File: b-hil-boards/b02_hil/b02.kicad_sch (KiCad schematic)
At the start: 43 parts, among them J1 Conn_01x12_Socket, J2 Conn_01x06_Socket, K1 Relay_DPDT, K2 Relay_DPDT, K3 Relay_DPDT, K4 Relay_DPDT, SW1 SW_Push, U1 MAX485E, U2 ULN2003, U3 ADuM1412, U4 ESP32_C3_SuperMini, U5 OLED-128x64-I2C, U6 74LVC2G34, U7 AMS1117-3.3

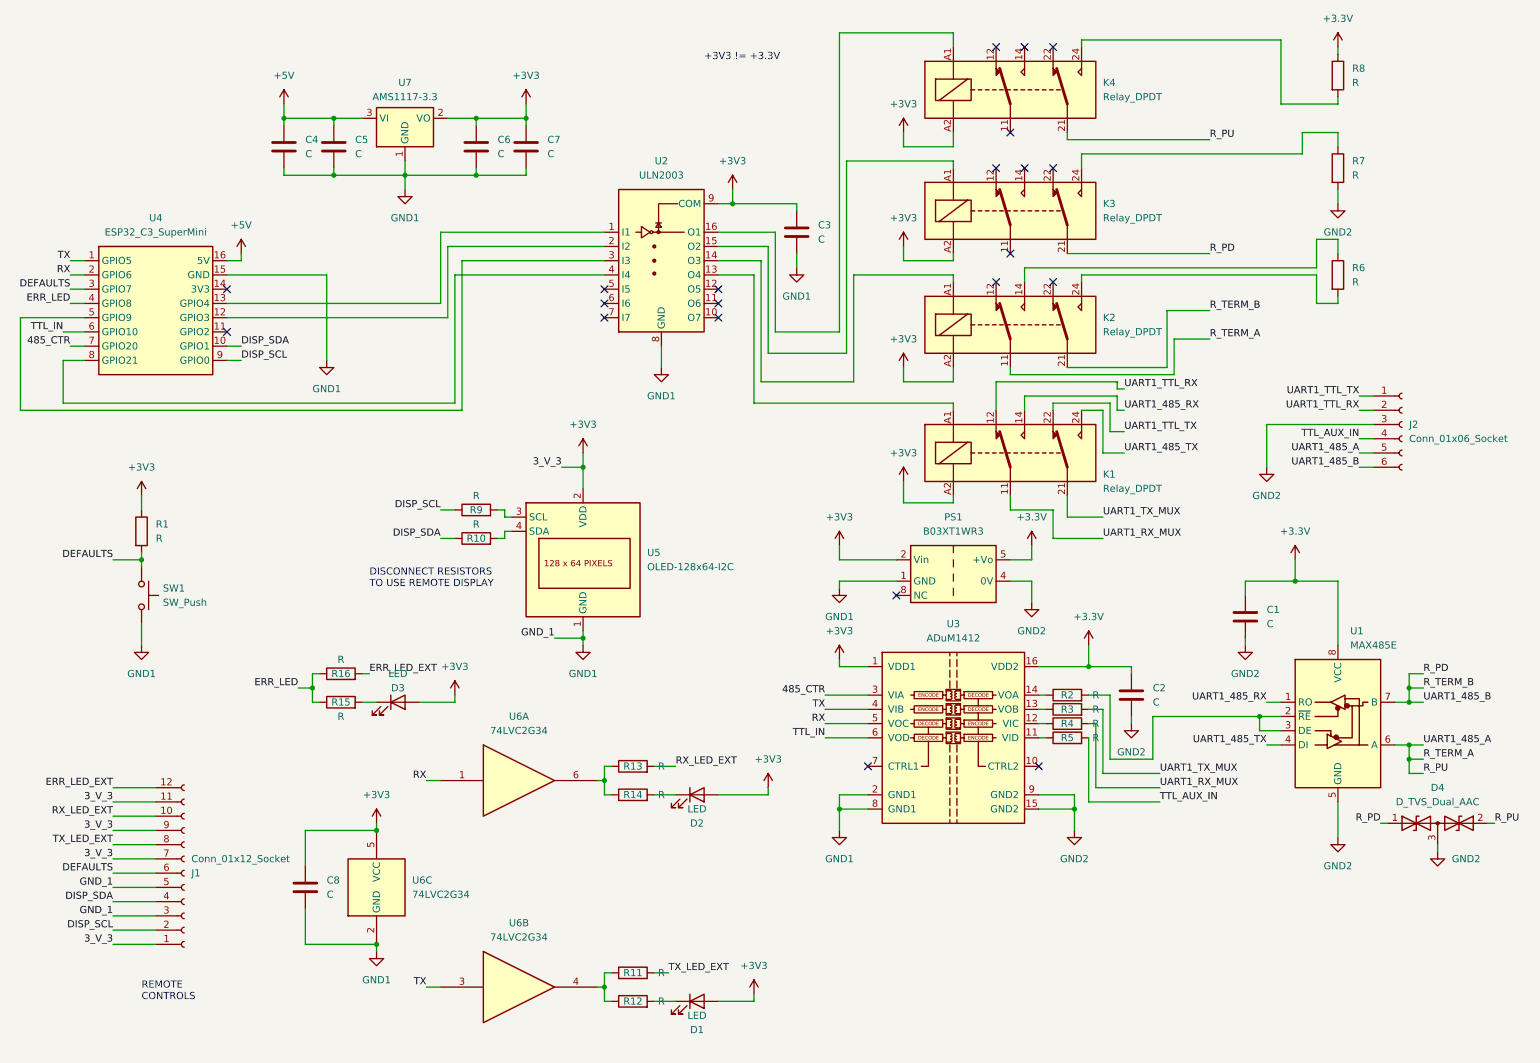
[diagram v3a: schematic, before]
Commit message: B02: add tri-state buffer and re-route PCB
Add 74HCT541 tri-state buffer to the schematic and re-route b02.kicad_pcb
to integrate the new device. Update project layout, refresh FreeRouting
exchange files (b02.dsn, b02.rules, b02.ses), and rotate KiCad automatic
backup archives.
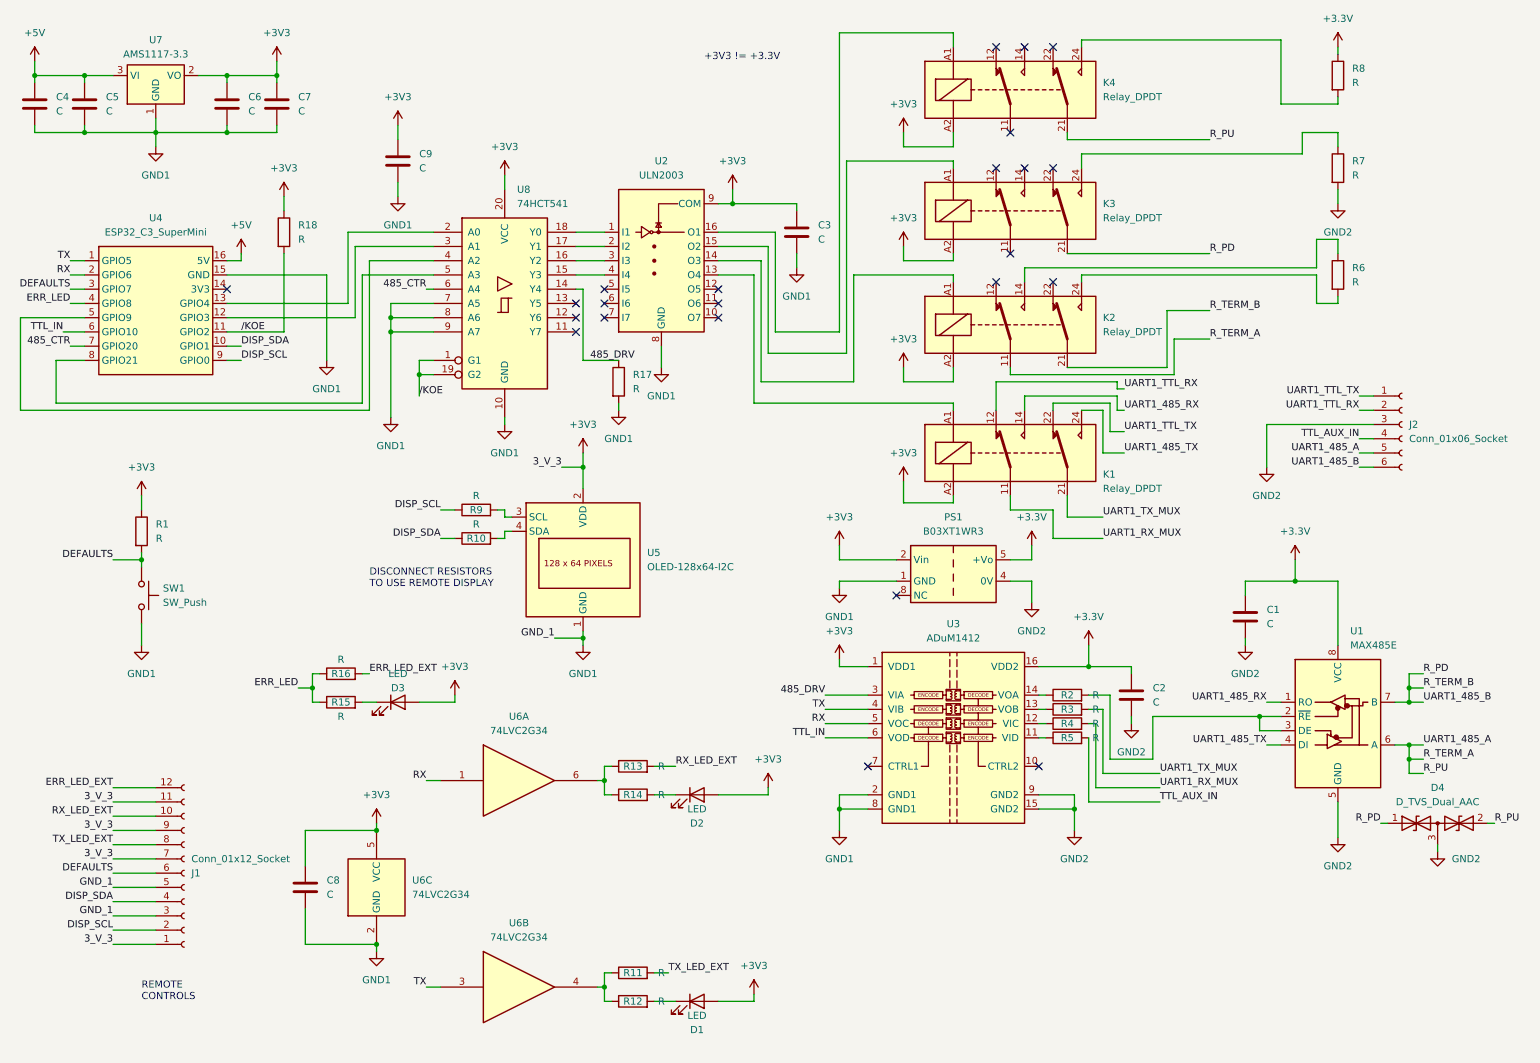
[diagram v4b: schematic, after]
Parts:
- added C9: C, Capacitor_SMD:C_0805_2012Metric_Pad1.18x1.45mm_HandSolder, symbol Device:C
- added R17, R18: R, Resistor_SMD:R_0805_2012Metric_Pad1.20x1.40mm_HandSolder, symbol Device:R
- added U8: 74HCT541, Package_SO:TSSOP-20_4.4x6.5mm_P0.65mm, symbol 74xx:74HCT541
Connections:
- net +3V3: now also C9.1, R18.1, U8.20 (VCC)
- net 485_CTR: now also U8.6 (A4); no longer U3.3 (VIA)
- net GND1: now also C9.2, R17.2, U8.10 (GND), U8.7 (A5), U8.8 (A6), U8.9 (A7)
- net at U2.1 (I1): now also U8.18 (Y0); no longer U4.13 (GPIO4)
- net at U2.2 (I2): now also U8.17 (Y1); no longer U4.12 (GPIO3)
- net at U2.3 (I3): now also U8.16 (Y2); no longer U4.5 (GPIO9)
- net at U2.4 (I4): now also U8.15 (Y3); no longer U4.8 (GPIO21)
- net /KOE: now reaches U4.11 (GPIO2)
- net /KOE: now also R18.2, U8.1 (G1), U8.19 (G2)
- new net: U4.12 (GPIO3), U8.3 (A1)
- new net: U4.13 (GPIO4), U8.2 (A0)
- new net: U4.5 (GPIO9), U8.4 (A2)
- new net: U4.8 (GPIO21), U8.5 (A3)
- new net 485_DRV: R17.1, U3.3 (VIA), U8.14 (Y4)
- no-connect marks 21 -> 23
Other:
- moved on the sheet: C4, C5, C6, C7, U7
